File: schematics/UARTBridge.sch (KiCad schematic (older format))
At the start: 5 parts, among them U14 CP2102, U17 SP0503BAHT

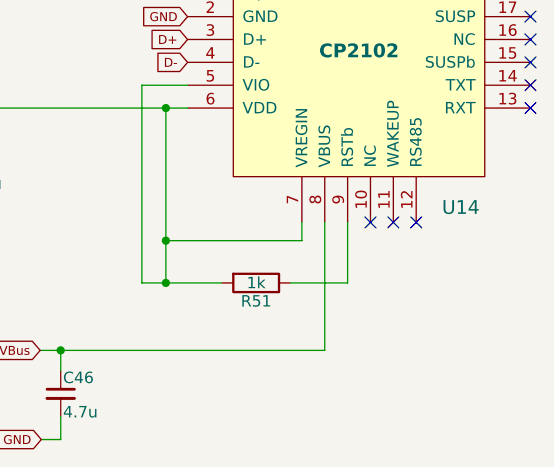
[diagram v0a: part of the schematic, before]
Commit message: update: added spacing with more test points
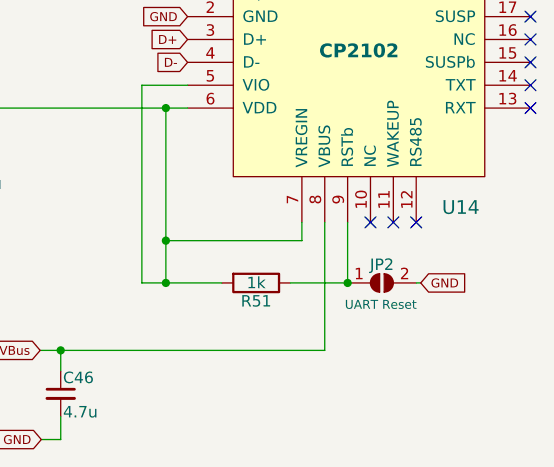
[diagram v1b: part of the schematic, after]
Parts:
- added JP2: UART Reset, Connectors:GS2, symbol Jumper:SolderJumper_2_Open
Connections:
- net GND: now also JP2.2 (B)
- net at R51.1, U14.9 (RSTb): now also JP2.1 (A)
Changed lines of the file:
@@
 Wire Wire Line
 	5075 4865 5075 5050
+$Comp
+L Jumper:SolderJumper_2_Open JP2
+U 1 1 5C9A740E
+P 6020 5050
+F 0 "JP2" H 6020 5130 50  0000 C CNN
+F 1 "UART Reset" H 6015 4955 39  0000 C CNN
+F 2 "Connectors:GS2" H 6020 5050 50  0001 C CNN
+F 3 "~" H 6020 5050 50  0001 C CNN
+	1    6020 5050
+	1    0    0    -1
+$EndComp
+Connection ~ 5870 5050
+Text GLabel 6190 5050 2    39   Input ~ 0
+GND
+Wire Wire Line
+	6190 5050 6170 5050
 $EndSCHEMATC

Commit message: docs: verrification of BoM
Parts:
- R51: value 1k -> 1K
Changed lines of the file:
@@
 AR Path="/5C4FD460/5C5002F8" Ref="R51"  Part="1"
 F 0 "R51" V 5550 5050 50  0000 C CNN
-F 1 "1k" V 5470 5050 50  0000 C CNN
+F 1 "1K" V 5470 5050 50  0000 C CNN
 F 2 "Resistors_SMD:R_0603" V 5400 5050 50  0001 C CNN
 F 3 "" H 5470 5050 50  0001 C CNN
